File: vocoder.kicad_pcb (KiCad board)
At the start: 2 copper layers, 42.8 x 31.9 mm, 39 parts, among them J1 AudioJack4, J2 Conn_01x02_Socket, J3 Conn_01x02_Pin, J4 USB_C_Receptacle_USB2.0_16P, Q1 Q_NPN_BCE, Q2 Q_NPN_BCE, Q3 Q_NPN_BCE, SW1 SW_SPDT, SW2 SW_Push, SW3 SW_Push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

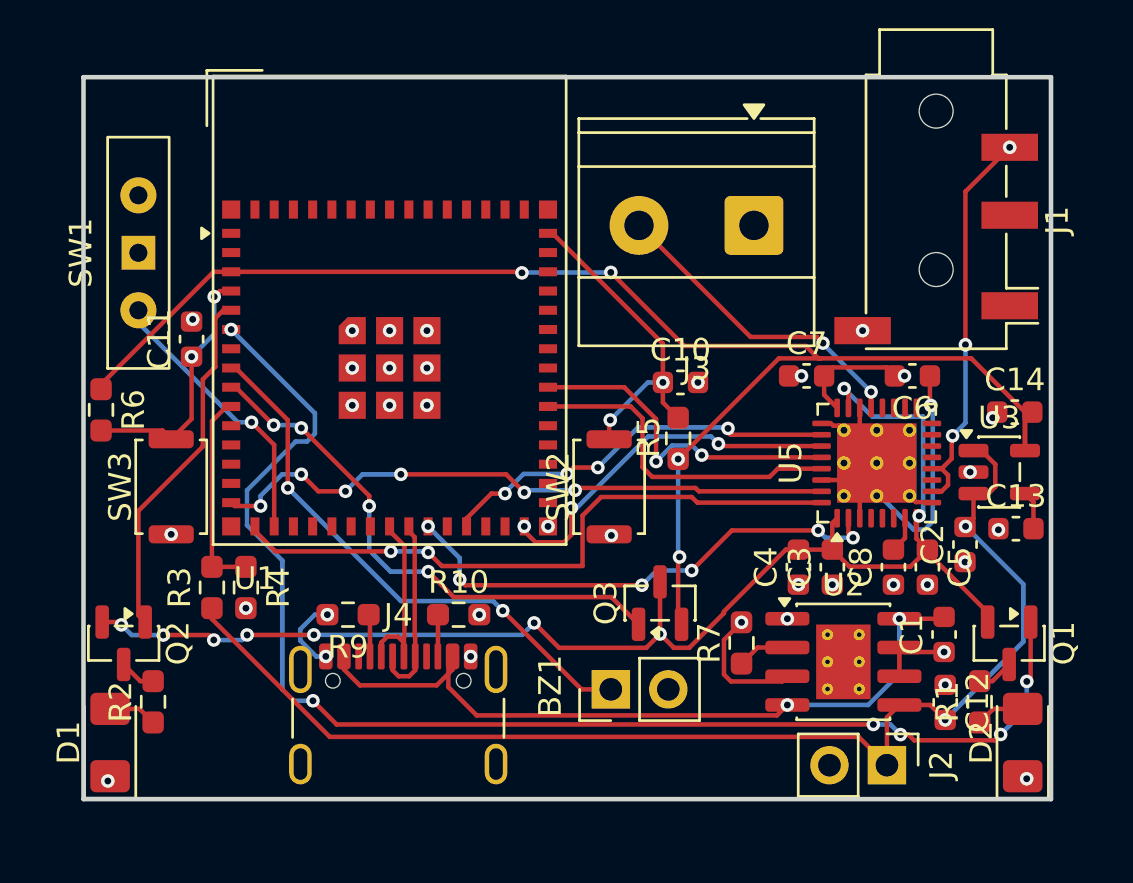
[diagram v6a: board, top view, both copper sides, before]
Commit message: added debug led's
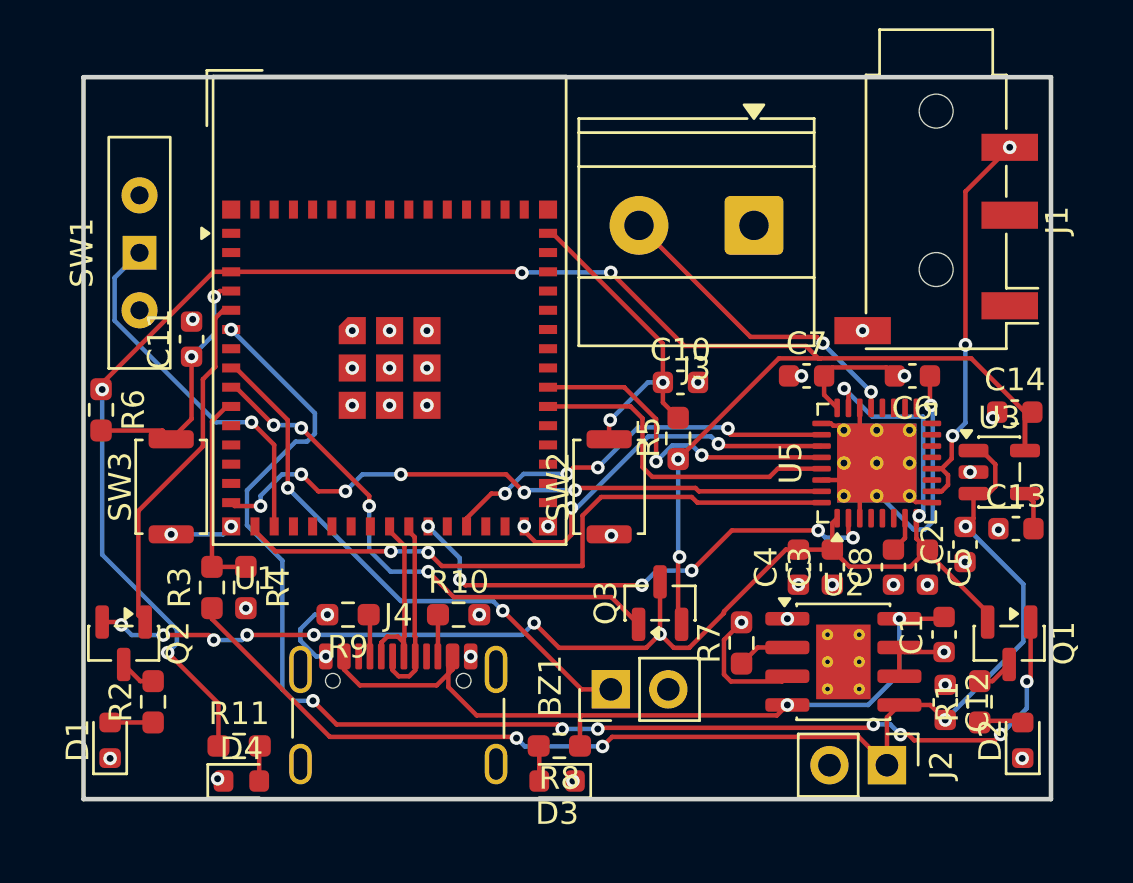
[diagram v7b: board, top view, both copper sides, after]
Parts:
- added D3: LED BLUE, LED_SMD:LED_0603_1608Metric, F.Cu at (146.8, 95.0)
- added D4: LED GREEN, LED_SMD:LED_0603_1608Metric, F.Cu at (132.9, 95.0)
- added R11: 100, Resistor_SMD:R_0603_1608Metric_Pad0.98x0.95mm_HandSolder, F.Cu at (132.8, 93.5)
- added R8: 220, Resistor_SMD:R_0603_1608Metric_Pad0.98x0.95mm_HandSolder, F.Cu at (146.9, 93.5)
- D1, D2: footprint LED_SMD:LED_1206_3216Metric_Pad1.42x1.75mm_HandSolder -> LED_SMD:LED_0603_1608Metric
- moved D1 0.10 mm to (127.1, 93.2)
- moved D2 0.10 mm to (167.4, 93.2)
- moved SW1 0.05 mm to (128.4, 71.7)
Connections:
- SW1 pad 1: unconnected-(SW1-A-Pad1) -> SWITCH_INPUT
- SW1 pad 2: SWITCH_INPUT -> unconnected-(SW1-B-Pad2)
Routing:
- net 3V3_PRE: track 64.8 -> 83.0 mm, vias 4 -> 6
- net SWITCH_INPUT: track 12.4 -> 16.4 mm
- net GND: track 34.2 -> 37.1 mm, vias 36 -> 39
- net Net-(D4-A): track 0.00 -> 1.56 mm
- net Net-(D3-A): track 0.00 -> 1.56 mm
- net USB_5V: track 33.6 -> 35.0 mm
- net BATT+: track 54.1 -> 54.5 mm, vias 2 -> 4
- net LED_RIGHT: track 57.9 -> 58.1 mm, vias 6 -> 8

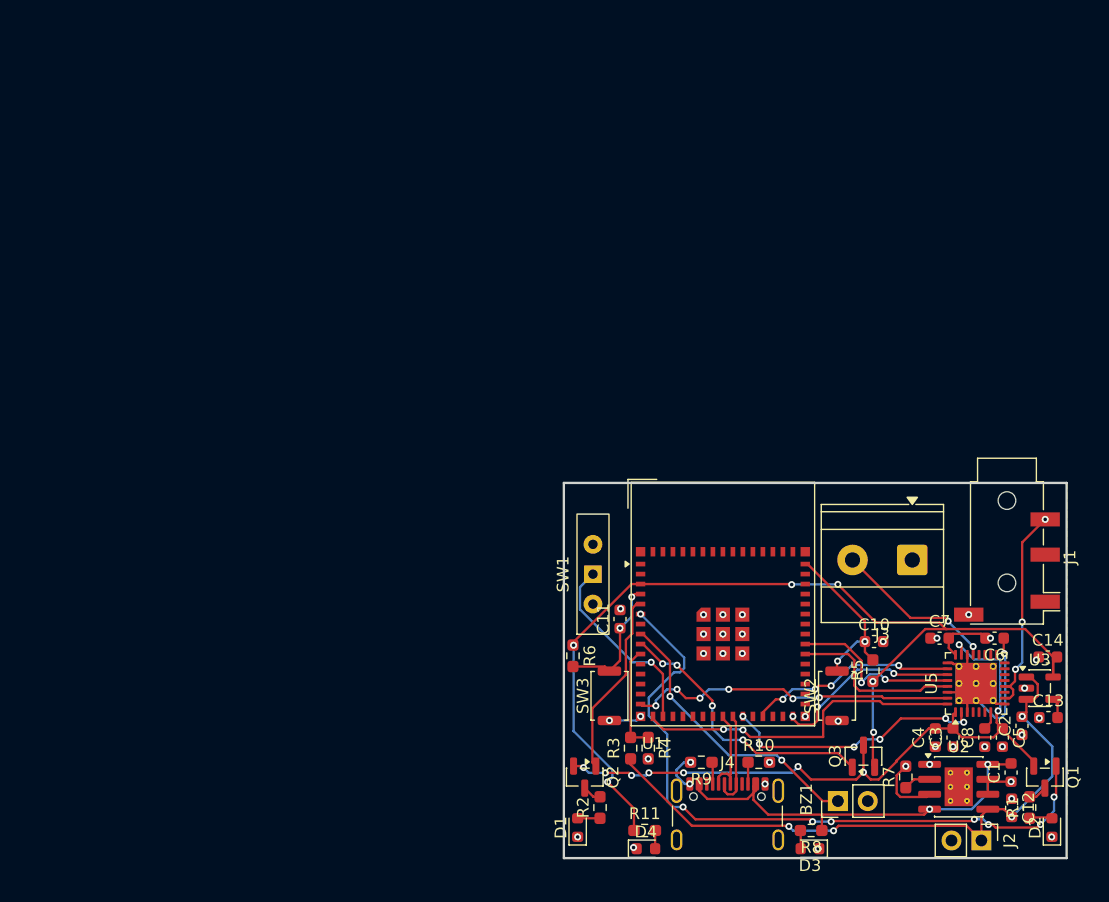
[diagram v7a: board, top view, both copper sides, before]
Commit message: working circuit without amplifier
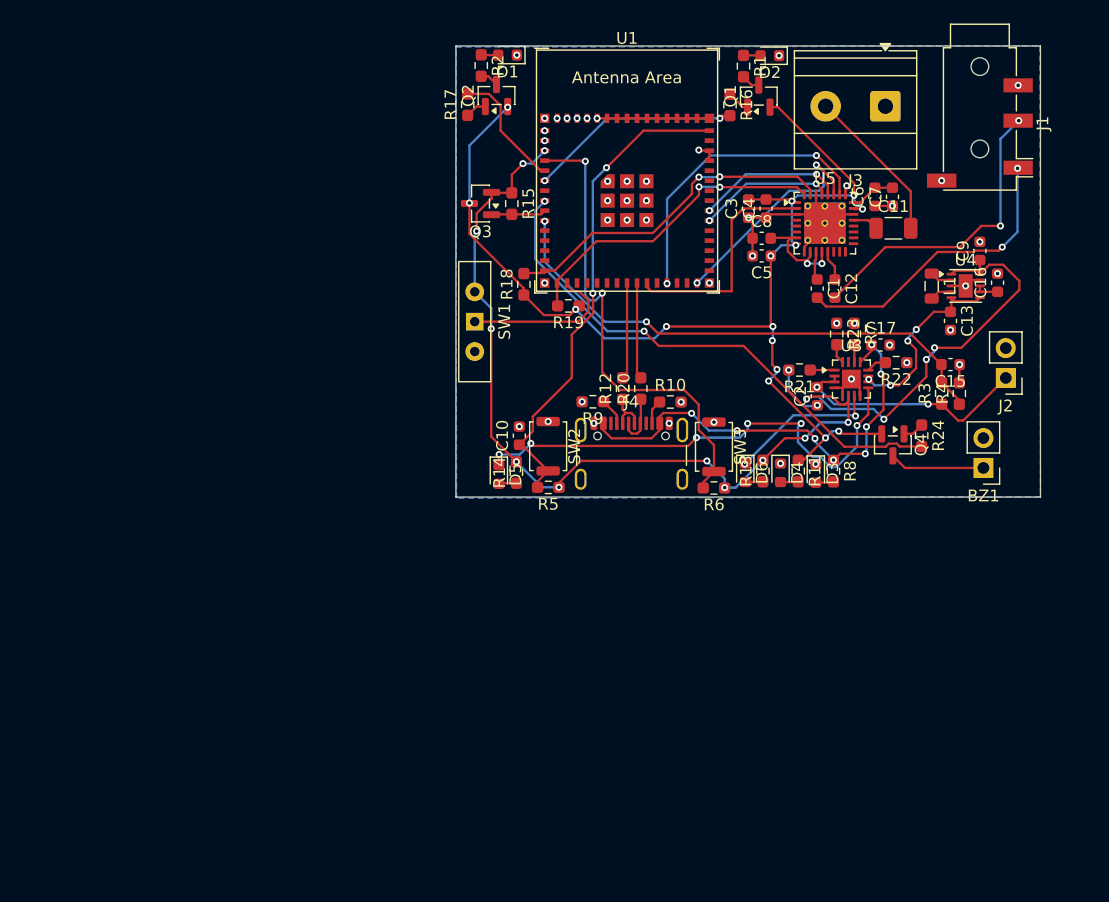
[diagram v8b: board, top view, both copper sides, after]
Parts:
- removed C14: 1u, Capacitor_SMD:C_0603_1608Metric
- removed U2: TP4056-42-ESOP8, Package_SO:SOIC-8-1EP_3.9x4.9mm_P1.27mm_EP2.41x3.3mm_ThermalVias
- added C15: 100n, Capacitor_SMD:C_0603_1608Metric, F.Cu at (158.8, 53.9)
- added C16: 0.1u, Capacitor_SMD:C_0603_1608Metric, F.Cu at (162.8, 46.9)
- added C17: 10u, Capacitor_SMD:C_0603_1608Metric, F.Cu at (152.8, 52.2)
- added C9: 10u, Capacitor_SMD:C_0603_1608Metric, F.Cu at (161.3, 44.2)
- added D5: LED RED, LED_SMD:LED_0603_1608Metric, F.Cu at (120.4, 63.2)
- added D6: LED GREEN, LED_SMD:LED_0603_1608Metric, F.Cu at (141.3, 63.1)
- added L1: 1.5uH, Inductor_SMD:L_0805_2012Metric, F.Cu at (157.2, 47.2)
- added Q4: Q_NPN_BCE, Package_TO_SOT_SMD:SOT-23, F.Cu at (153.9, 60.7)
- added R12: 27, Resistor_SMD:R_0603_1608Metric_Pad0.98x0.95mm_HandSolder, F.Cu at (130.9, 55.9)
- added R13: 1k, Resistor_SMD:R_0603_1608Metric_Pad0.98x0.95mm_HandSolder, F.Cu at (142.8, 62.9)
- added R14: 1k, Resistor_SMD:R_0603_1608Metric_Pad0.98x0.95mm_HandSolder, F.Cu at (121.9, 63.1)
- added R15: 100k, Resistor_SMD:R_0603_1608Metric_Pad0.98x0.95mm_HandSolder, F.Cu at (121.5, 40.2)
- added R16: 1k, Resistor_SMD:R_0603_1608Metric_Pad0.98x0.95mm_HandSolder, F.Cu at (140.1, 31.8)
- added R17: 1k, Resistor_SMD:R_0603_1608Metric_Pad0.98x0.95mm_HandSolder, F.Cu at (117.8, 31.8)
- added R18: 4.7k, Resistor_SMD:R_0603_1608Metric_Pad0.98x0.95mm_HandSolder, F.Cu at (122.5, 47.1)
- added R19: 4.7k, Resistor_SMD:R_0603_1608Metric_Pad0.98x0.95mm_HandSolder, F.Cu at (126.3, 48.9)
- added R20: 27, Resistor_SMD:R_0603_1608Metric_Pad0.98x0.95mm_HandSolder, F.Cu at (132.5, 55.9)
- added R21: 10k, Resistor_SMD:R_0603_1608Metric_Pad0.98x0.95mm_HandSolder, F.Cu at (146.0, 54.4)
- added R22: 910, Resistor_SMD:R_0603_1608Metric_Pad0.98x0.95mm_HandSolder, F.Cu at (154.2, 53.7)
- added R23: 910, Resistor_SMD:R_0603_1608Metric_Pad0.98x0.95mm_HandSolder, F.Cu at (149.1, 51.3)
- added R24: 1k, Resistor_SMD:R_0603_1608Metric_Pad0.98x0.95mm_HandSolder, F.Cu at (156.3, 59.9)
- added U4: TPS63031DSK, Package_SON:WSON-10-1EP_2.5x2.5mm_P0.5mm_EP1.2x2mm, F.Cu at (160.1, 47.2)
- C1: value 10u -> 2.2u
- C11: value 0.1u -> 10u; footprint Capacitor_SMD:C_0603_1608Metric -> Capacitor_SMD:C_1206_3216Metric
- C12: value 1u -> 2.2u
- C13: value 1u -> 10u
- D1, D2: value LED -> LED RED
- Q3: value Q_NPN_BCE -> AO3401A
- R11: value 100 -> 220
- R3: value 10k -> 100k
- R7: value 1.2k -> 72k
- U1: footprint RF_Module:ESP32-S2-MINI-1 -> PCM_Espressif:ESP32-S3-MINI-1
- U3: value TPS73633DBV -> BQ24074RGT; footprint Package_TO_SOT_SMD:SOT-23-5 -> Package_DFN_QFN:VQFN-16-1EP_3x3mm_P0.5mm_EP1.6x1.6mm
- moved D2 69.9 mm to (143.4, 27.6), turned to 180 degrees
- moved R1 67.6 mm to (141.2, 28.5), turned to -90 degrees
- moved D1 65.9 mm to (121.1, 27.6), turned to 180 degrees
- moved R2 63.9 mm to (118.9, 28.5), turned to -90 degrees
- moved Q1 62.8 mm to (142.5, 31.1), turned to 90 degrees
- moved Q2 58.4 mm to (120.2, 31.0), turned to 90 degrees
- moved Q3 57.2 mm to (118.8, 40.2), turned to 180 degrees
- moved C3 48.2 mm to (141.6, 40.6)
- moved C4 47.2 mm to (143.1, 40.6)
- moved C12 46.6 mm to (149.0, 47.4)
- moved C8 46.5 mm to (142.7, 43.1), turned to 0 degrees
- moved C5 45.8 mm to (142.7, 44.6), turned to 180 degrees
- moved C1 44.3 mm to (147.5, 47.4), turned to -90 degrees
- moved U5 41.2 mm to (148.1, 41.9), turned to 0 degrees
- moved C11 40.5 mm to (153.9, 42.3), turned to 0 degrees
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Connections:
- BZ1 pad 1: BUZZER -> Net-(BZ1-+)
- C1 pad 1: GND -> Net-(U5-LINN)
- C1 pad 2: USB_5V -> Net-(C1-Pad2)
- C11 pad 1: BOOT -> Net-(U5-MONOOUT)
- C11 pad 2: GND -> Net-(J3-Pin_2)
- C12 pad 1: GND -> Net-(U5-RINN)
- C12 pad 2: BATT+ -> Net-(C12-Pad2)
- C13 pad 1: GND -> Net-(U4-EN)
- C13 pad 2: Net-(U3-NR) -> GND
- C8 pad 2: Net-(U5-CM) -> CM
- J1 pad R1: unconnected-(J1-PadR1) -> Net-(C12-Pad2)
- J1 pad R2: Net-(U5-LINP) -> GND
- J1 pad T: unconnected-(J1-PadT) -> Net-(C1-Pad2)
- J4 pad A6: USB+ -> Net-(J4-D+-PadA6)
- J4 pad A7: USB- -> Net-(J4-D--PadA7)
- J4 pad B6: USB+ -> Net-(J4-D+-PadA6)
- J4 pad B7: USB- -> Net-(J4-D--PadA7)
- Q1 pad 1: LED_RIGHT -> Net-(Q1-B)
- Q2 pad 1: LED_LEFT -> Net-(Q2-B)
- R11 pad 1: 3V3_PRE -> 3V3
- R7 pad 1: Net-(U2-PROG) -> GND
- R7 pad 2: GND -> Net-(U3-TMR)
- SW1 pad 2: unconnected-(SW1-B-Pad2) -> 3V3_PRE
- U3 pad 1: BATT+ -> Net-(U3-TS)
- U3 pad 2: GND -> BATT+
- U3 pad 4: Net-(U3-NR) -> GND
- U3 pad 5: 3V3_PRE -> GND
- U5 pad 10: Net-(U5-LINP) -> CM
- U5 pad 11: unconnected-(U5-LINN-Pad11) -> Net-(U5-LINN)
- U5 pad 12: Net-(U5-LINP) -> CM
- U5 pad 13: unconnected-(U5-RINN-Pad13) -> Net-(U5-RINN)
- U5 pad 21: Net-(J3-Pin_2) -> Net-(U5-MONOOUT)
- U5 pad 7: Net-(U5-CM) -> CM
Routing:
- net Net-(D5-K): track 0.00 -> 41.9 mm, vias 0 -> 6
- net 3V3: track 59.6 -> 99.7 mm, vias 9 -> 15
- net LED_RIGHT: track 58.1 -> 18.0 mm, vias 8 -> 2
- net BATT_READ: track 9.06 -> 44.9 mm, vias 0 -> 2
- net BATT+: track 54.5 -> 20.9 mm, vias 4 -> 2
- net BOOT: track 11.2 -> 40.4 mm
- net EN: track 14.5 -> 41.3 mm
- net Net-(C12-Pad2): track 0.00 -> 26.2 mm, vias 0 -> 2
- net Net-(C1-Pad2): track 0.00 -> 25.4 mm, vias 0 -> 2
- net 3V3_PRE: track 83.0 -> 106.0 mm, vias 6 -> 15
- net BUZZER: track 24.4 -> 45.0 mm
- net 3V3_SWITCH: track 23.7 -> 4.67 mm, vias 4 -> 0
- net Net-(U5-LINP): track 17.5 -> 0.00 mm, vias 3 -> 0
- net Net-(U4-EN): track 0.00 -> 16.5 mm, vias 0 -> 4
- net Net-(D6-K): track 0.00 -> 13.0 mm, vias 0 -> 2
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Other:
- board size 42.8 x 31.9 mm -> 49.7 x 38.4 mm
